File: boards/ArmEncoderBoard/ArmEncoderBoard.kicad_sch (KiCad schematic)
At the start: 25 parts, among them J1 Conn_01x05, Q1 SS8050, Q2 SS8050, U1 SN74LVC2G17DBVR, U2 AS5045B

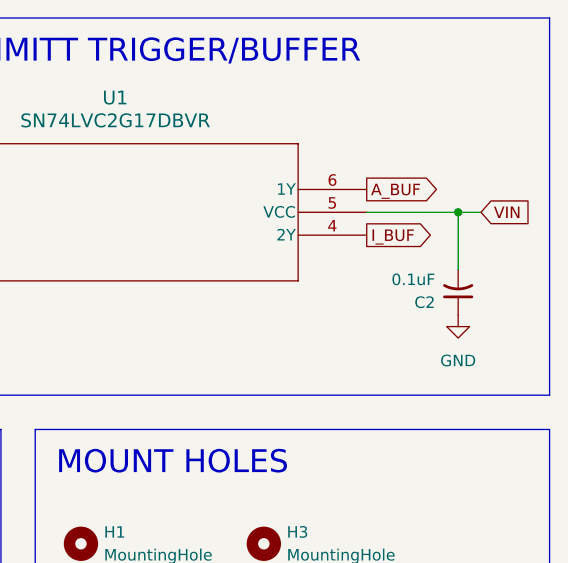
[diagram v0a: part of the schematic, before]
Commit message: Pre-flight on two encoder boards
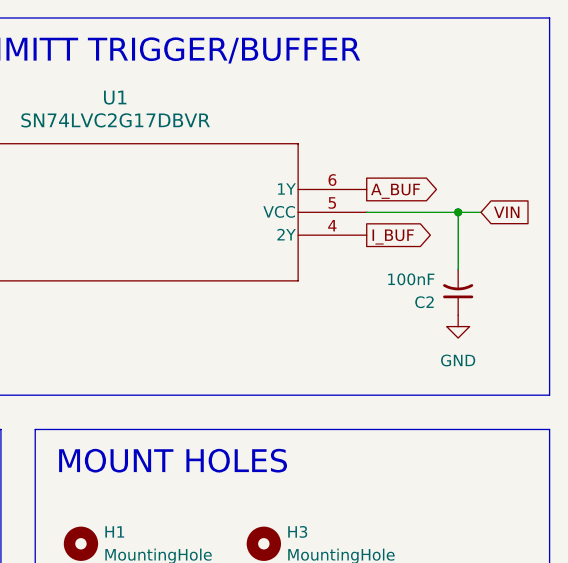
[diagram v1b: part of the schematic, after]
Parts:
- C2: value 0.1uF -> 100nF
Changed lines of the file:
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@@
 			)
 		)
-		(property "Value" "0.1uF"
+		(property "Value" "100nF"
 			(at 220.98 46.8631 0)
 			(effects

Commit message: Order arm encoder board, update bom
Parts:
- D1: footprint LedBlue:YLED0603B -> LedBlue:150080BS75000_Modified; LCSC C19171394 -> C6067133
- D2: footprint LedRed:YLED0603R -> LedRed:NCD0603R1; LCSC C19171390 -> C84263
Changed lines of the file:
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@@
 			)
 		)
-		(property "Footprint" "LedRed:YLED0603R"
+		(property "Footprint" "LedRed:NCD0603R1"
 			(at 176.53 139.7 0)
 			(effects
@@
 			)
 		)
-		(property "LCSC" "C19171390"
+		(property "LCSC" "C84263"
 			(at 174.9425 133.35 0)
 			(effects
@@
 			)
 		)
-		(property "Footprint" "LedBlue:YLED0603B"
+		(property "Footprint" "LedBlue:150080BS75000_Modified"
 			(at 176.53 116.84 0)
 			(effects
@@
 			)
 		)
-		(property "LCSC" "C19171394"
+		(property "LCSC" "C6067133"
 			(at 174.9425 110.49 0)
 			(effects

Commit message: Update main and leg board
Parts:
- added C5: 10nF, Capacitor10nF:GRM1885C1H103JA01D, symbol Device:C_Small_US
- added CR3: BAT54, EnvelopeDiode:BAT54WS-7-F, symbol EnvelopeDiode:BAT54WS-7-F
- added D3, D4: LEDRED, LedRed:NCD0603R1, symbol Device:LED
- added R10, R11: 10K, Resistor10K:CRCW060310K0FKEA, symbol Device:R_US
- added R12, R13: 1K, Resistor1K:RCG06031K00FKEA, symbol Device:R_US
- added R9: 100K, Resistor100K:CRCW0603100KFKEA, symbol Device:R_US
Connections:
- net A_BUF: now also C5.1; no longer CR1.2
- net GND: now also CR3.2, R9.1
- net VIN: now also D3.2 (A), D4.2 (A), R10.1, R11.1
- net I_BASE: now reaches Q2.1 (B), R8.1
- net MAGINC: now reaches U2.1 (~{MagINC})
- net MAGINC: now also R10.2, R13.2
- net MAGDEC: now reaches U2.2 (~{MagDEC})
- net MAGDEC: now also R11.2, R12.2
- net A_BASE: now reaches Q1.1 (B), R5.1
- new net: D3.1 (K), R13.1
- new net: D4.1 (K), R12.1
- new net A_PULSE: C5.2, CR1.2, CR3.1, R9.2
- no-connect marks 4 -> 2
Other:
- note added: "HOLES"
- note added: "MAG DEC"
- note added: "MAG INC"
- note removed: "MOUNT HOLES"
- note removed: "TRANSISTORS"
- moved on the sheet: C1, C2, C3, C4, CR1, CR2, D1, D2, H1, H2, H3, H4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

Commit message: Clean up and document boards
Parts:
- added R14, R15: 470K, Resistor470K:RC0603FR-07470KL, symbol Device:R_US
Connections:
- net A_BASE: now also R14.2
- net GND: now also R14.1, R15.1
- net I_BASE: now also R15.2
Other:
- note added: "MOUNT HOLES"
- note removed: "HOLES"
- moved on the sheet: D1, D2, H2, H3, H4, Q1, Q2, R3, R4

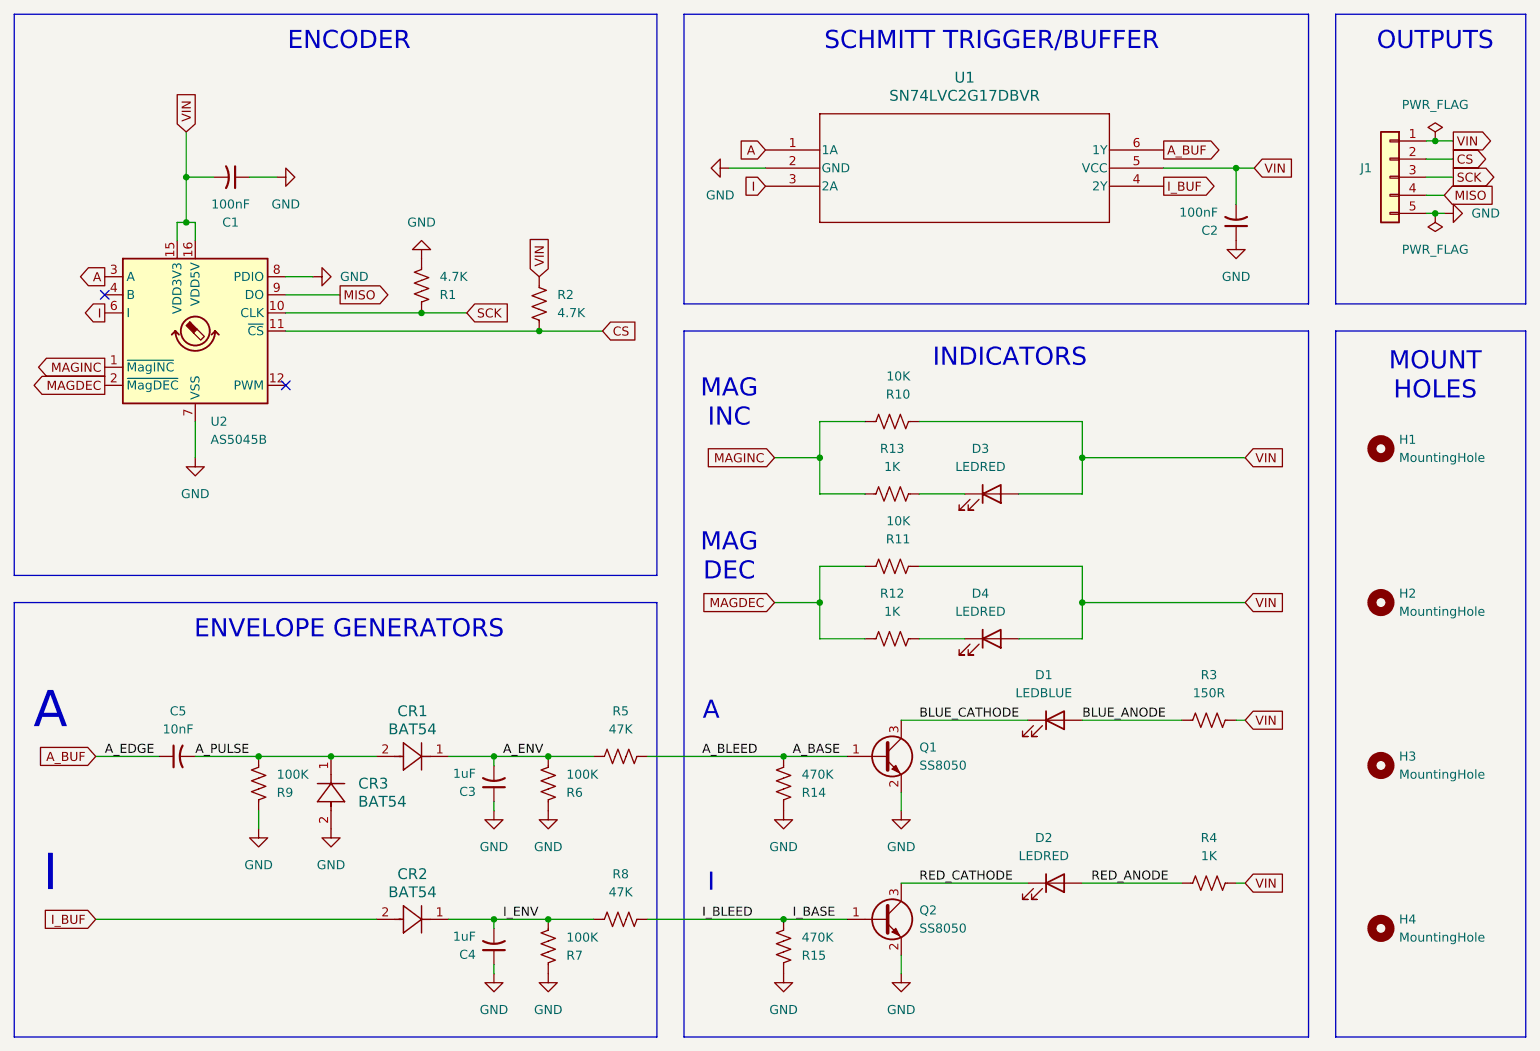
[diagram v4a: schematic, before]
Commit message: Complete documentation for encoder boards
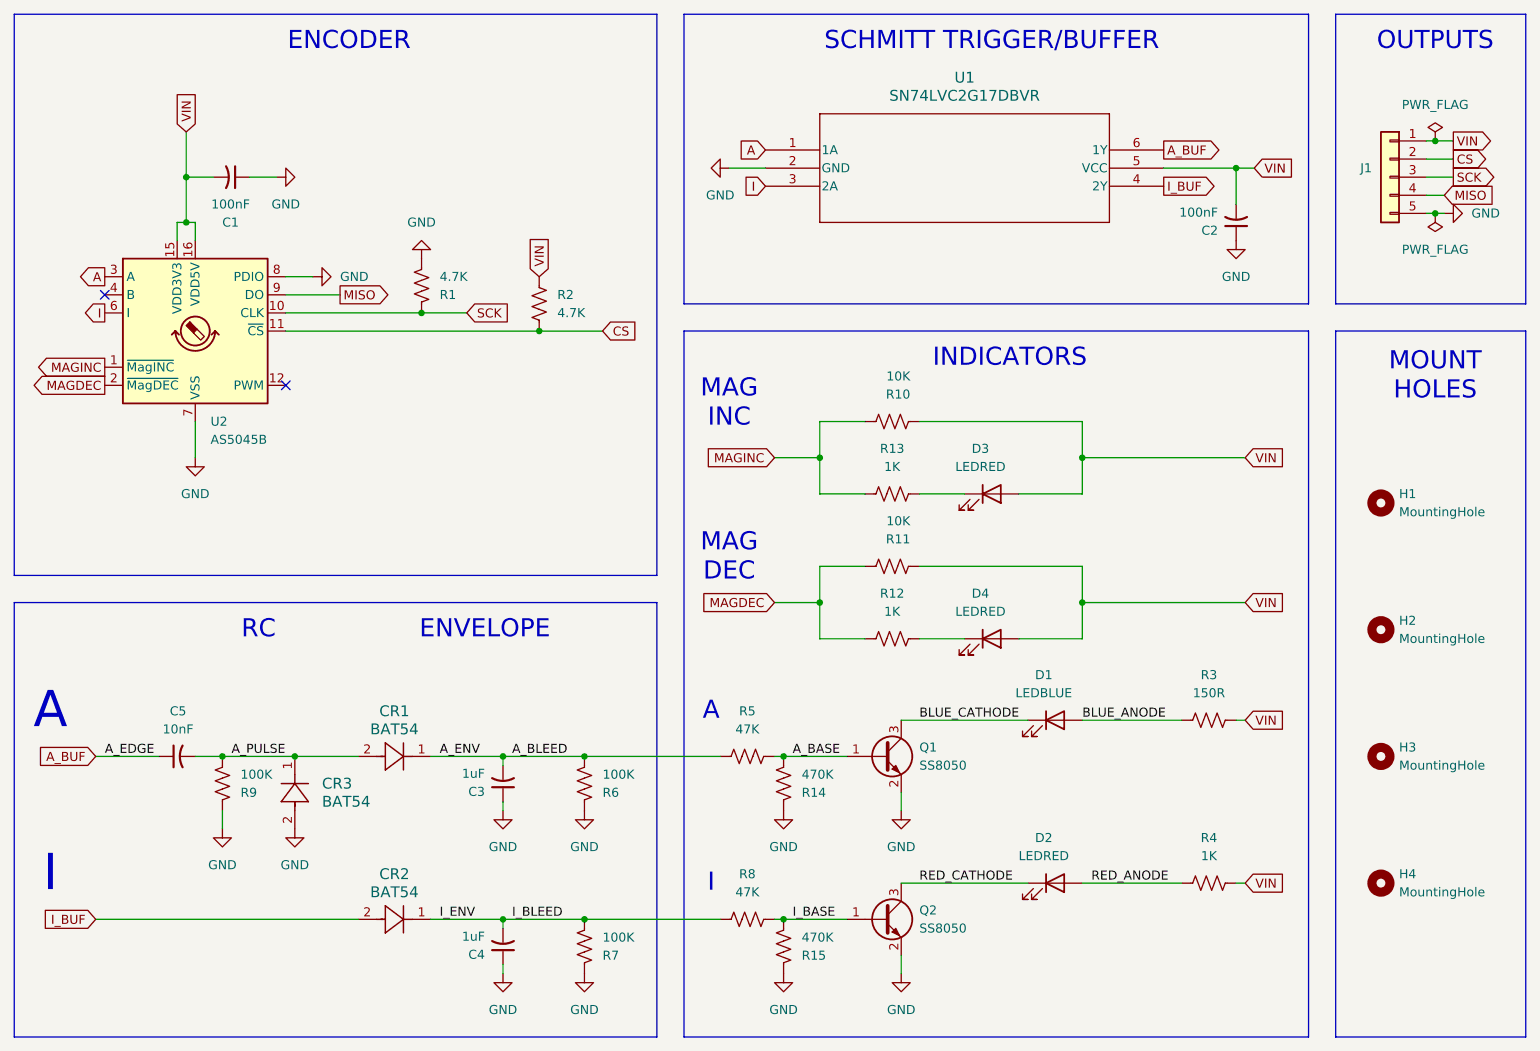
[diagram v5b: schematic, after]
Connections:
- net A_ENV renamed A_BLEED
- net I_ENV renamed I_BLEED
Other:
- note added: "ENVELOPE"
- note added: "RC"
- note removed: "ENVELOPE GENERATORS"
- moved on the sheet: C3, C4, CR1, CR2, CR3, H1, H2, H3, H4, R5, R6, R7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
